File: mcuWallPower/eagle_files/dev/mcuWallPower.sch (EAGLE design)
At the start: 3 parts, among them P1 CR2032

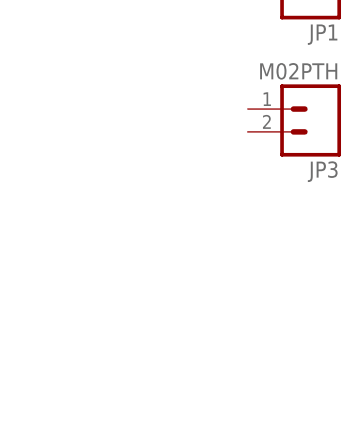
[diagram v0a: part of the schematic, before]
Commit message: Added USB mini connector to board along with other components. Todo: Replace USB mini connector with USB micro B connector. Looks like I'll need to make a custom footprint.
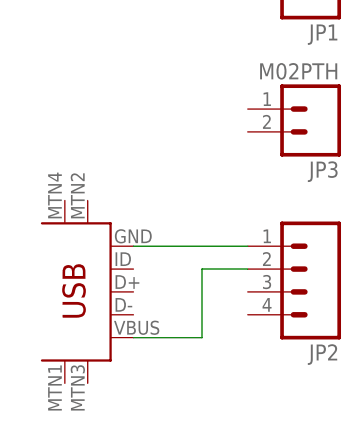
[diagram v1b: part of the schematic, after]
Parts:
- added JP2: (no value), SparkFun-Connectors:M04PTH
- added U1: USB-MINIB-5PIN, SparkFun-Connectors:USB-MINIB-5PIN
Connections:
- new net N$3: JP2.1, U1.GND
- new net N$4: JP2.2, U1.VBUS
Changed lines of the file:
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@@
 <part name="JP1" library="SparkFun-Connectors" deviceset="M04" device="PTH"/>
 <part name="JP3" library="SparkFun-Connectors" deviceset="M02" device="PTH"/>
+<part name="U1" library="SparkFun-Connectors" deviceset="USB-MINIB" device="-5PIN"/>
+<part name="JP2" library="SparkFun-Connectors" deviceset="M04" device="PTH"/>
 </parts>
 <sheets>
@@
 <instance part="JP1" gate="G$1" x="45.72" y="78.74" rot="R180"/>
 <instance part="JP3" gate="G$1" x="48.26" y="60.96" rot="R180"/>
+<instance part="U1" gate="G$1" x="25.4" y="45.72" rot="R180"/>
+<instance part="JP2" gate="G$1" x="45.72" y="43.18" rot="R180"/>
 </instances>
 <busses>
@@
 </segment>
 </net>
+<net name="N$3" class="0">
+<segment>
+<pinref part="U1" gate="G$1" pin="GND"/>
+<pinref part="JP2" gate="G$1" pin="1"/>
+<wire x1="27.94" y1="45.72" x2="40.64" y2="45.72" width="0.1524" layer="91"/>
+</segment>
+</net>
+<net name="N$4" class="0">
+<segment>
+<pinref part="U1" gate="G$1" pin="VBUS"/>
+<wire x1="27.94" y1="35.56" x2="35.56" y2="35.56" width="0.1524" layer="91"/>
+<wire x1="35.56" y1="35.56" x2="35.56" y2="43.18" width="0.1524" layer="91"/>
+<pinref part="JP2" gate="G$1" pin="2"/>
+<wire x1="35.56" y1="43.18" x2="40.64" y2="43.18" width="0.1524" layer="91"/>
+</segment>
+</net>

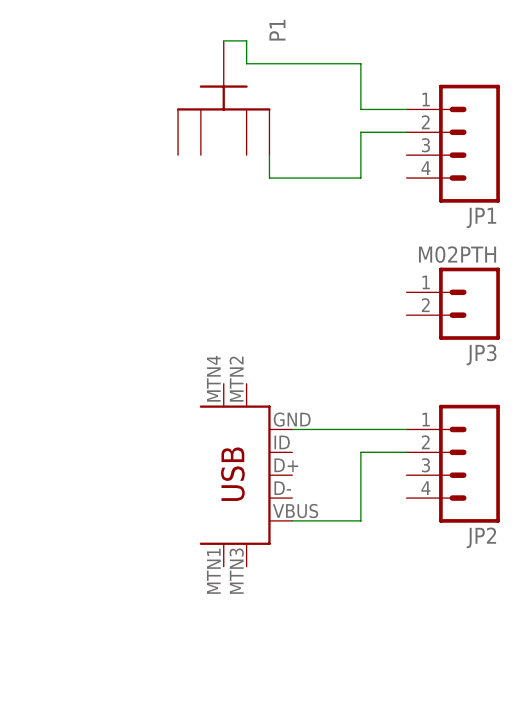
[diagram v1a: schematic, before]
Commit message: mcuWallPower schematic and board updated. Ready for fitting.
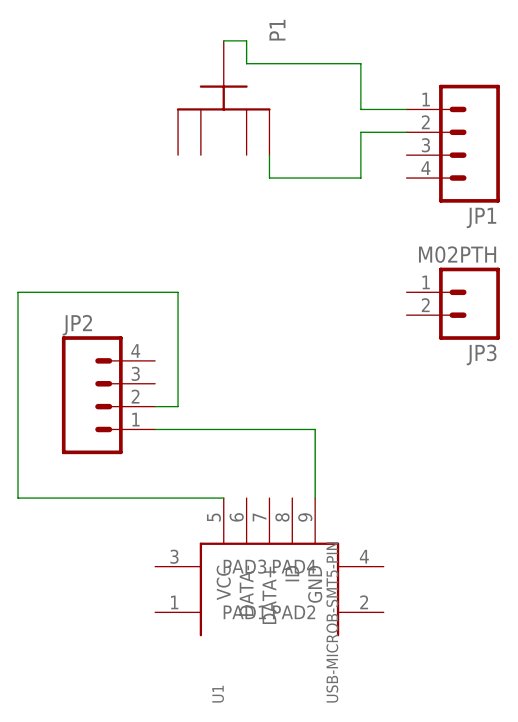
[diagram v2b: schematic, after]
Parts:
- U1: value USB-MINIB-5PIN -> USB-MICROB-SMT5-PIN; device SparkFun-Connectors:USB-MINIB-5PIN -> freddyLibr:USB-MICROB-SMT5-PIN
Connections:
- net N$4: now also U1.VCC; no longer U1.VBUS
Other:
- moved on the sheet: JP2
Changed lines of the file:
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@@
 <part name="JP1" library="SparkFun-Connectors" deviceset="M04" device="PTH"/>
 <part name="JP3" library="SparkFun-Connectors" deviceset="M02" device="PTH"/>
-<part name="U1" library="SparkFun-Connectors" deviceset="USB-MINIB" device="-5PIN"/>
 <part name="JP2" library="SparkFun-Connectors" deviceset="M04" device="PTH"/>
+<part name="U1" library="freddyLibr" deviceset="USB-MICROB-SMT" device="5-PIN"/>
 </parts>
 <sheets>
@@
 <instance part="JP1" gate="G$1" x="45.72" y="78.74" rot="R180"/>
 <instance part="JP3" gate="G$1" x="48.26" y="60.96" rot="R180"/>
-<instance part="U1" gate="G$1" x="25.4" y="45.72" rot="R180"/>
-<instance part="JP2" gate="G$1" x="45.72" y="43.18" rot="R180"/>
+<instance part="JP2" gate="G$1" x="7.62" y="48.26"/>
+<instance part="U1" gate="G$1" x="25.4" y="27.94" rot="R90"/>
 </instances>
 <busses>
@@
 <net name="N$3" class="0">
 <segment>
+<wire x1="30.48" y1="38.1" x2="30.48" y2="45.72" width="0.1524" layer="91"/>
+<pinref part="JP2" gate="G$1" pin="1"/>
+<wire x1="30.48" y1="45.72" x2="12.7" y2="45.72" width="0.1524" layer="91"/>
 <pinref part="U1" gate="G$1" pin="GND"/>
-<pinref part="JP2" gate="G$1" pin="1"/>
-<wire x1="27.94" y1="45.72" x2="40.64" y2="45.72" width="0.1524" layer="91"/>
 </segment>
 </net>
 <net name="N$4" class="0">
 <segment>
-<pinref part="U1" gate="G$1" pin="VBUS"/>
-<wire x1="27.94" y1="35.56" x2="35.56" y2="35.56" width="0.1524" layer="91"/>
-<wire x1="35.56" y1="35.56" x2="35.56" y2="43.18" width="0.1524" layer="91"/>
+<wire x1="20.32" y1="38.1" x2="-2.54" y2="38.1" width="0.1524" layer="91"/>
+<wire x1="-2.54" y1="38.1" x2="-2.54" y2="60.96" width="0.1524" layer="91"/>
+<wire x1="-2.54" y1="60.96" x2="15.24" y2="60.96" width="0.1524" layer="91"/>
+<pinref part="U1" gate="G$1" pin="VCC"/>
 <pinref part="JP2" gate="G$1" pin="2"/>
-<wire x1="35.56" y1="43.18" x2="40.64" y2="43.18" width="0.1524" layer="91"/>
+<wire x1="12.7" y1="48.26" x2="15.24" y2="48.26" width="0.1524" layer="91"/>
+<wire x1="15.24" y1="48.26" x2="15.24" y2="60.96" width="0.1524" layer="91"/>
 </segment>
 </net>
